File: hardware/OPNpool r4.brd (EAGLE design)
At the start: 63 x 58 mm, 16 parts, among them J2 RS485-TERM-SPTAF, J3 ESP-JTAG-2X05, SW1 Factory (5 sec), U1 MAX3485CSA+

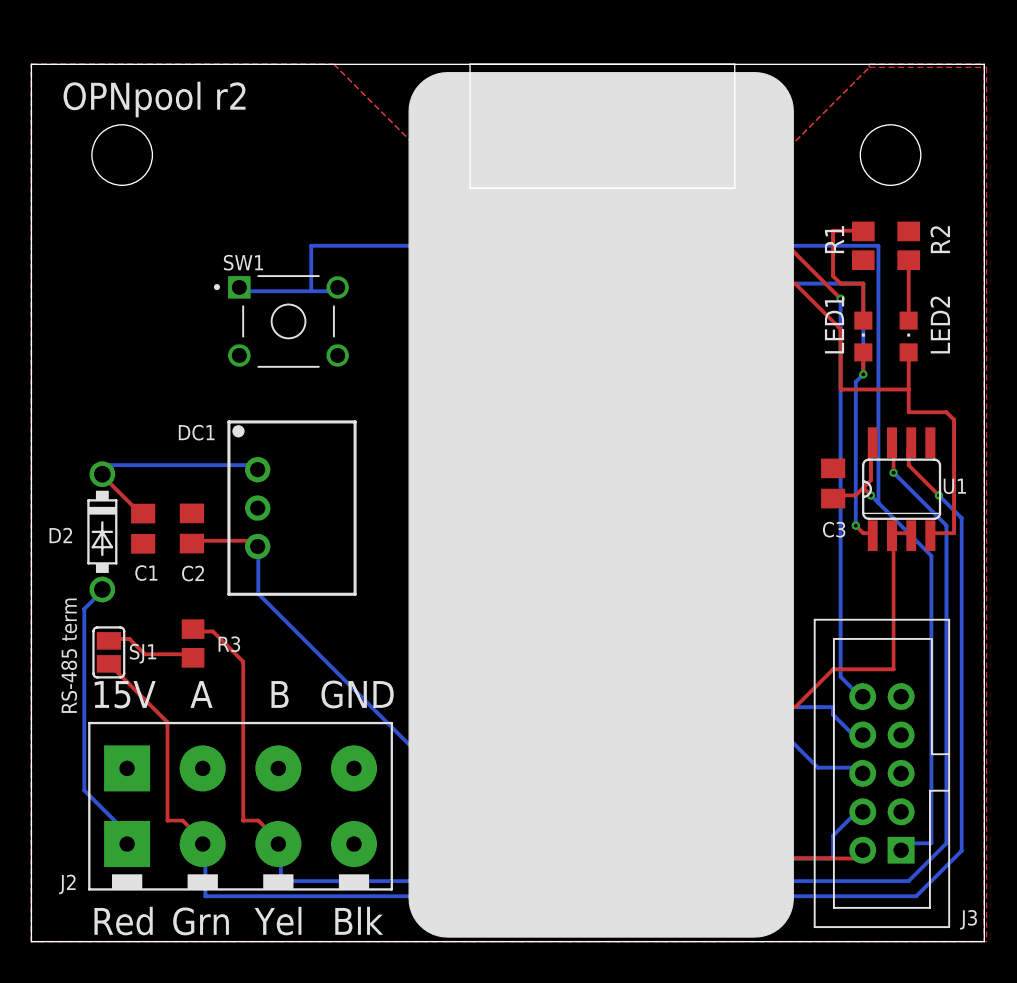
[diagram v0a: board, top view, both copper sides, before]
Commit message: switch to esp32-c6-devkitc-1 module
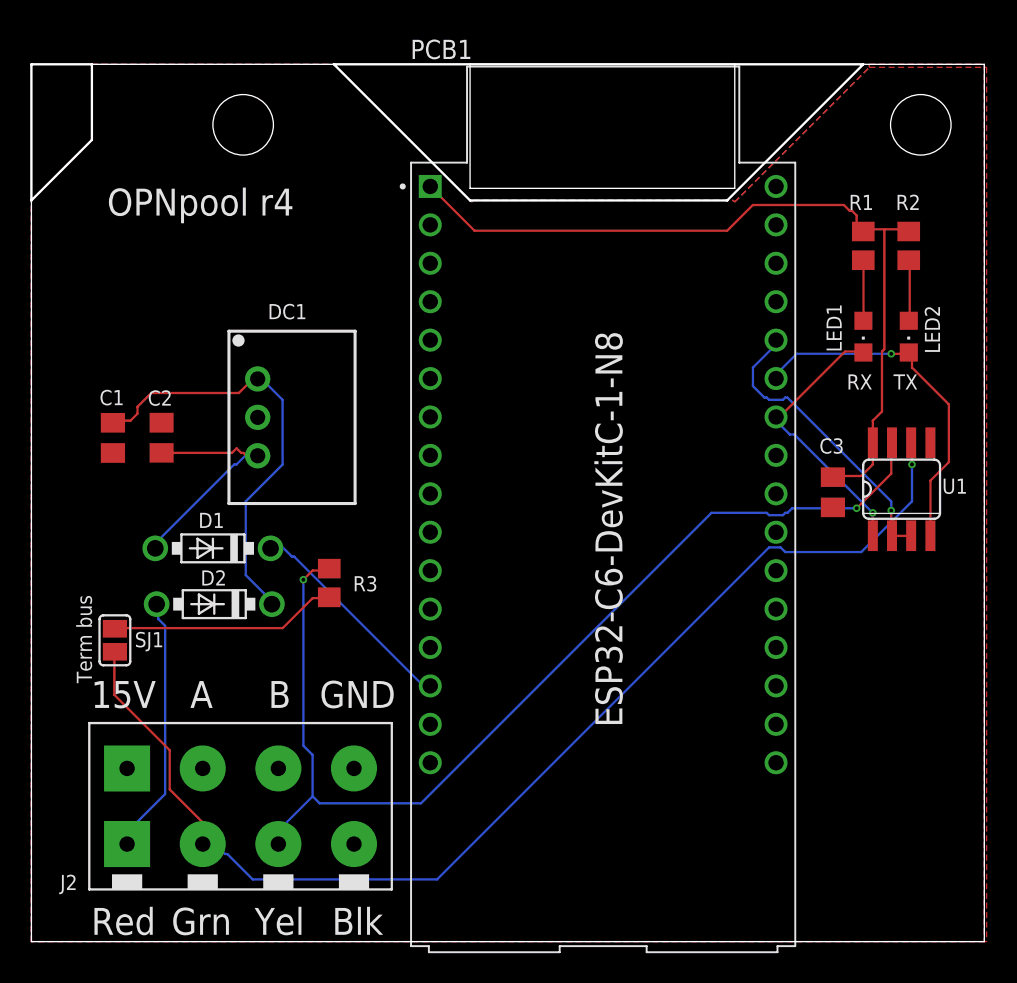
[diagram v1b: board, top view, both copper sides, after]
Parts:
- removed J3: ESP-JTAG-2X05, Coert Vonk:2X05_SHROUDED
- removed SW1: Factory (5 sec), 1-1825910-4:TE_1-1825910-4
- added D1: 1N5818, Coert Vonk:DO41-7.6
- PCB1: value LOLIN-D32 -> ESP32-C6-DEVKITC-1-N8; device Coert Vonk:LOLIN-D32 -> Coert-Vonk:MODULE_ESP32-C6-DEVKITC-1-N8
- moved R3 9.85 mm to (19.7, 23.7)
- moved D2 8.81 mm to (12.1, 22.3), turned to 180 degrees
- moved C2 6.32 mm to (8.61, 33.3)
- moved C1 6.32 mm to (5.39, 33.3)
- moved DC1 6.00 mm to (17.5, 34.7)
- moved PCB1 4.07 mm to (37.8, 25.6), turned to 0 degrees
- moved SJ1 0.89 mm to (5.52, 19.9)
- moved C3 0.58 mm to (53.0, 29.7), turned to 270 degrees
- turned LED1 to 180 degrees
- turned LED2 to 180 degrees
- turned R2 to 90 degrees
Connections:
- removed net JTAG_!RST: J3.10, PCB1.RS
- removed net JTAG_CK: J3.4, PCB1.13
- removed net JTAG_DI: J3.8, PCB1.12
- removed net JTAG_DO: J3.6, PCB1.15
- removed net JTAG_MS: J3.2, PCB1.14
- removed net N$3: PCB1.0, SW1.1, SW1.2
- removed net RTS: PCB1.27, U1.2, U1.3
- removed net RX2: LED1.A, PCB1.25, U1.1
- removed net TX: LED2.A, PCB1.26, U1.4
- new net N$4: D1.C, PCB1.5V0
- new net RTS1: PCB1.IO23, U1.2, U1.3
- new net RX1: LED1.C, PCB1.IO21, U1.1
- new net TX1: LED2.C, PCB1.IO22, U1.4
- net 3V3: now also R1.2, R2.2; no longer J3.1
- net GND: now also PCB1.GND@3; no longer J3.3, J3.5, J3.7, J3.9, PCB1.34, PCB1.VN, PCB1.VP, R1.1, R2.1, SW1.3, SW1.4
- net N$1: now also LED1.A, R1.1; no longer LED1.C, R1.2
- net N$2: now also LED2.A, R2.1; no longer LED2.C, R2.2
- net VOUT: now also D1.A; no longer PCB1.BAT
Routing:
- net TX: track 64.5 -> 0.00 mm
- net RX2: track 58.5 -> 0.00 mm, vias 2 -> 0
- net JTAG_!RST: track 56.2 -> 0.00 mm, vias 1 -> 0
- net N$3: track 54.6 -> 0.00 mm, vias 1 -> 0
- net RTS: track 46.9 -> 0.00 mm
- net JTAG_MS: track 36.9 -> 0.00 mm
- net JTAG_CK: track 36.6 -> 0.00 mm
- net JTAG_DI: track 32.6 -> 0.00 mm
- net 3V3: track 81.6 -> 53.7 mm, vias 1 -> 0
- net TX1: track 0.00 -> 23.4 mm, vias 0 -> 1
- net B: track 93.4 -> 70.4 mm, vias 1 -> 2
- net A: track 98.5 -> 77.5 mm
- net RTS1: track 0.00 -> 19.8 mm, vias 0 -> 1
- net RX1: track 0.00 -> 18.3 mm, vias 0 -> 1
- net N$4: track 0.00 -> 14.4 mm
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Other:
- outline, holes or cut-outs redrawn
- board text added: "OPNpool r4"
- board text added: "RX"
- board text added: "TX"
- board text added: "Term bus"
- board text added: "https://github.com/cvonk/OPNpool_meets_ESPHome"
- board text removed: "OPNpool r2"
- board text removed: "RS-485 term"
- board text removed: "https://github.com/cvonk/OPNpool"
